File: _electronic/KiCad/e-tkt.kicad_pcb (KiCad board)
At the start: 2 copper layers, 96 x 72.7 mm, 96 parts, among them J1 USB4105-GF-A, Q1 SS8050-G, Q2 SS8050-G, U1 USB6B1, U2 AZ1117I-3.3, U3 FT231XS, U4 ESP32-WROOM-32

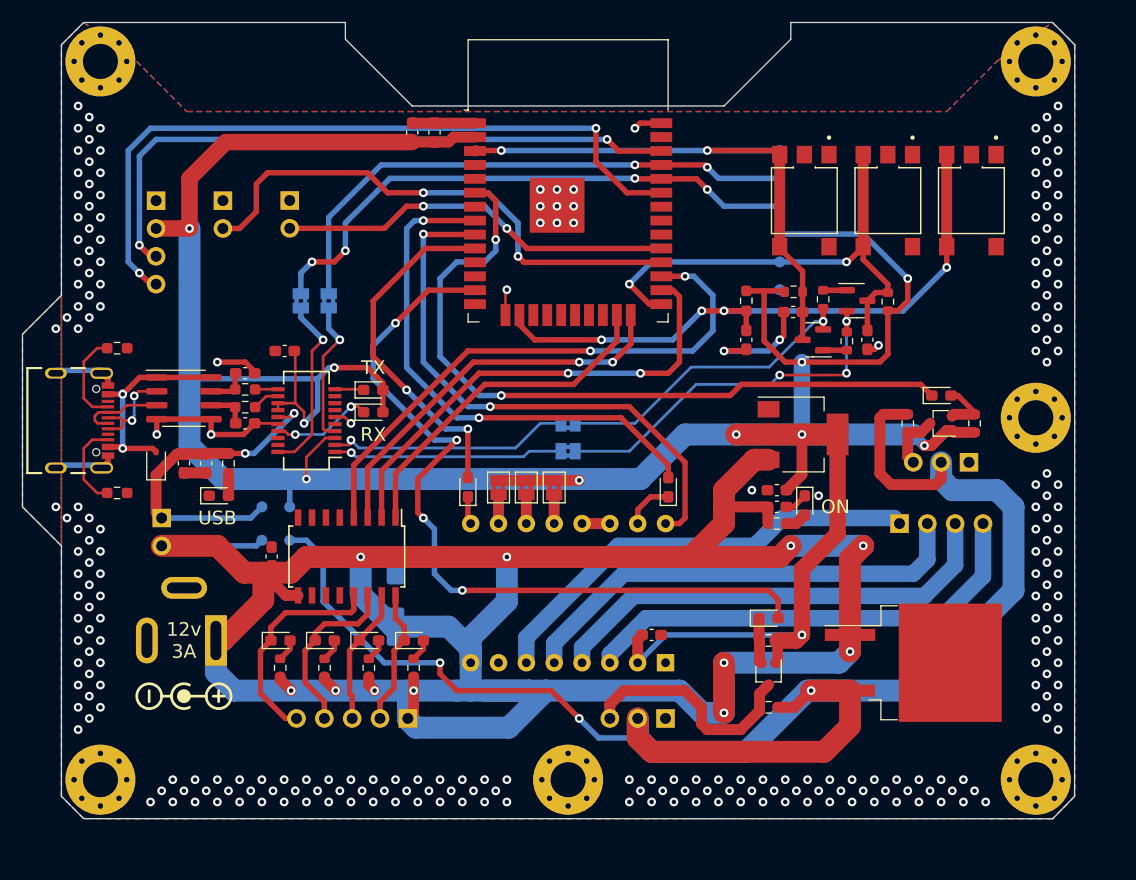
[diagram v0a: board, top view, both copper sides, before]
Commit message: board dimensions, taller
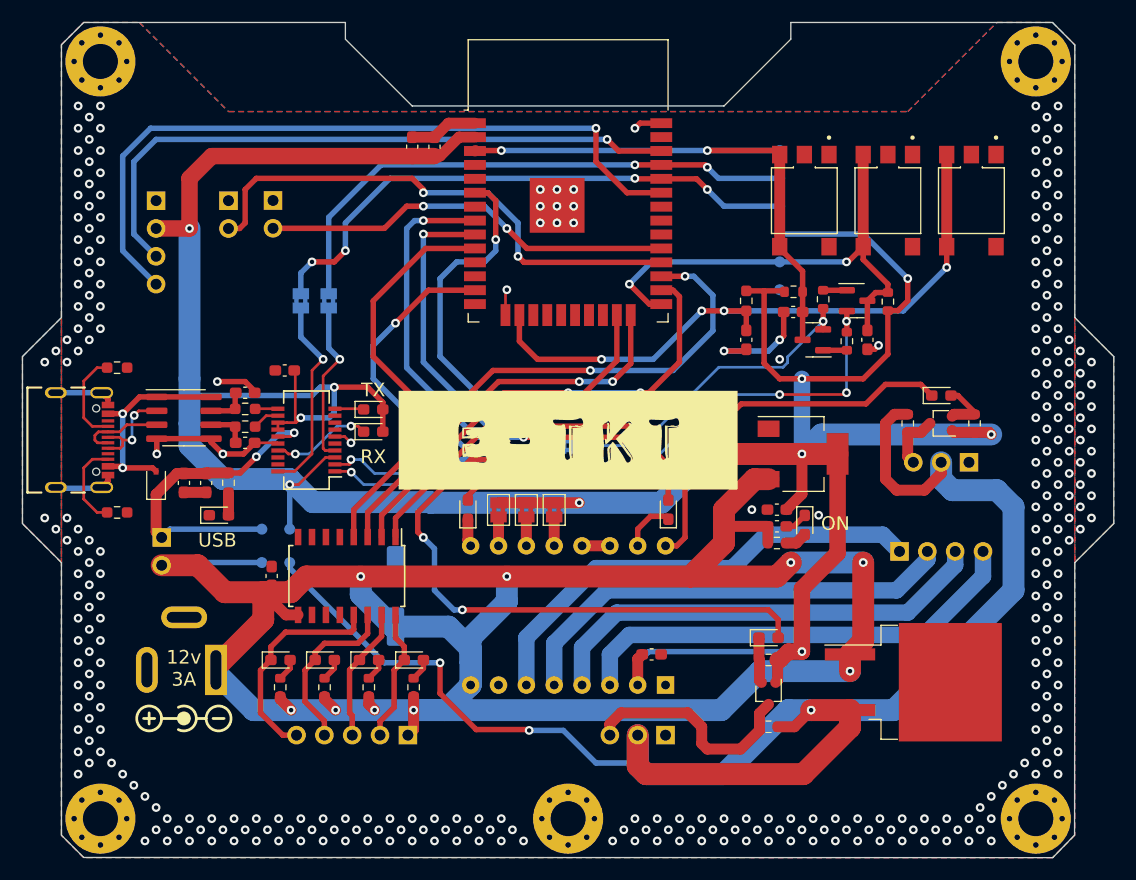
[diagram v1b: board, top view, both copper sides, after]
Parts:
- removed H5: MountingHole_Pad, MountingHole:MountingHole_3.2mm_M3_Pad_Via
- added G***: LOGO, LOGO, F.Cu at (178.3, -189.5)
- moved H3 3.56 mm to (221.0, -154.9)
- moved H4 3.56 mm to (135.6, -154.9)
- moved H6 3.56 mm to (178.3, -154.9)
- moved J_masterpower1 2.68 mm to (146.2, -168.5)
- moved J_17HS4023_1 2.54 mm to (208.5, -179.3)
- moved D1 2.04 mm to (187.5, -183.1)
- moved D4 2.04 mm to (169.2, -183.1)
- moved JP1 2.04 mm to (172.0, -183.1)
- moved JP2 2.04 mm to (174.5, -183.1)
- moved JP3 2.04 mm to (177.0, -183.1)
- moved JP6 2.03 mm to (178.3, -189.0)
- moved TP_12v1 2.03 mm to (150.4, -178.3)
- moved TP_3.3v1 2.03 mm to (152.9, -181.4)
- moved TP_5v1 2.03 mm to (150.4, -181.4)
- moved TP_6v1 2.03 mm to (152.9, -178.3)
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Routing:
- net +12V: track 243.5 -> 221.5 mm, vias 11 -> 9
- net +3.3V: track 292.5 -> 301.7 mm
- net IO25 NEMA ENA: track 31.7 -> 39.8 mm
- net IO14 SERVO: track 72.7 -> 80.6 mm
- net IO13 WIFI RST: track 57.2 -> 59.6 mm
- net DTR: track 34.4 -> 36.2 mm
- net Net-(A_DRIVER1-Pad6): track 41.1 -> 42.9 mm
- net Net-(JP4-Pad1): track 16.6 -> 18.3 mm
- net Net-(JP5-Pad1): track 13.2 -> 15.0 mm
- net IO5 LED END: track 36.3 -> 37.9 mm
- net IO34 HALL: track 67.2 -> 68.7 mm
- net RTS: track 28.4 -> 29.5 mm
- net IO33 NEMA DIR: track 51.1 -> 52.0 mm
- net IO32 NEMA STEP: track 47.9 -> 48.7 mm
- net IO16 ULN 4: track 51.3 -> 50.7 mm
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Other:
- board size 96 x 72.7 mm -> 99.6 x 76.2 mm
- board text added: "2022/07/09"
- board text added: "Andrei Speridião"
- board text added: "v0.9"
- board text removed: "Andrei Speridião 2022/07/09 v0.9"

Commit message: improved decouple caps position, routing
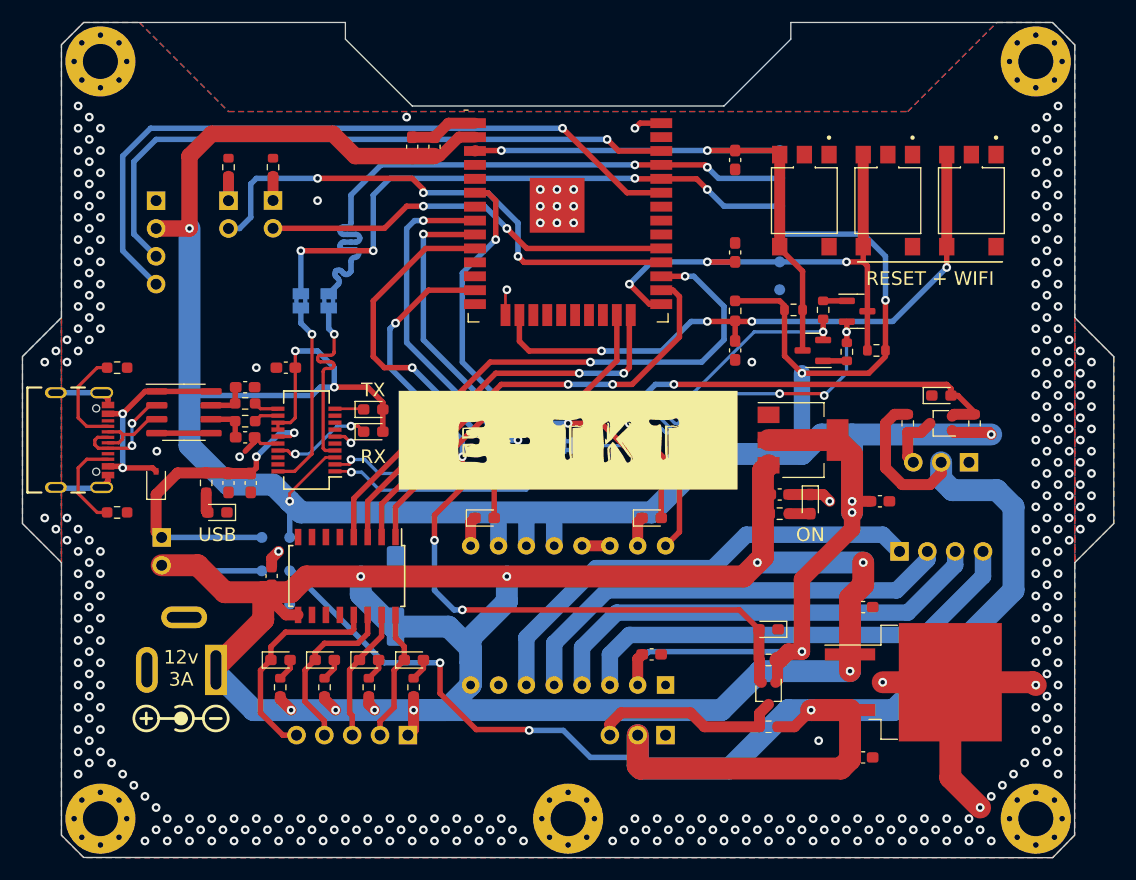
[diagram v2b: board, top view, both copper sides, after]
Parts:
- removed JP1, JP2, JP3: SolderJumper_2_Bridged, Jumper:SolderJumper-2_P1.3mm_Bridged2Bar_Pad1.0x1.5mm
- added C14: 0.33uF, Capacitor_SMD:C_0603_1608Metric_Pad1.08x0.95mm_HandSolder, F.Cu at (205.2, -174.2)
- added C17: 0.1uF, Capacitor_SMD:C_0603_1608Metric_Pad1.08x0.95mm_HandSolder, F.Cu at (205.2, -160.5)
- added R20: 0R, Resistor_SMD:R_0603_1608Metric, F.Cu at (147.3, -214.4)
- added R21: 0R, Resistor_SMD:R_0603_1608Metric, F.Cu at (151.4, -214.4)
- moved C4 14.8 mm to (193.5, -215.0), turned to 90 degrees
- moved C3 14.5 mm to (193.5, -206.6), turned to -90 degrees
- moved C11 9.43 mm to (206.8, -183.9), turned to 0 degrees
- moved R5 4.58 mm to (206.4, -197.7), turned to 180 degrees
- moved C15 4.06 mm to (149.4, -185.6)
- moved C2 4.06 mm to (147.3, -185.6)
- moved C10 2.92 mm to (197.6, -184.5)
- moved R2 2.69 mm to (197.6, -182.8)
- moved C6 2.03 mm to (164.1, -216.3)
- moved C7 2.03 mm to (166.1, -216.3)
- moved R6 2.03 mm to (145.3, -185.6)
- moved D11 1.97 mm to (200.4, -183.6)
- moved D1 1.70 mm to (185.9, -182.4), turned to 0 degrees
- moved D4 1.70 mm to (170.7, -182.4), turned to 0 degrees
- moved R1 1.65 mm to (198.9, -201.4)
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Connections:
- A_DRIVER1 pad 10: Net-(A_DRIVER1-Pad10) -> +3.3V
- A_DRIVER1 pad 11: Net-(A_DRIVER1-Pad11) -> +3.3V
- A_DRIVER1 pad 12: Net-(A_DRIVER1-Pad12) -> +3.3V
- D10 pad 1: Net-(D10-Pad1) -> GNDREF
- D9 pad 1: IO34 HALL -> GNDREF
- D9 pad 2: Net-(D9-Pad2) -> IO34 HALL
- J_LED_END1 pad 1: GNDREF -> Net-(J_LED_END1-Pad1)
- J_LED_PRESS1 pad 1: GNDREF -> Net-(J_LED_PRESS1-Pad1)
- Q_HALL1 pad 2: Net-(D9-Pad2) -> IO34 HALL
- Q_SERVO1 pad 2: Net-(D10-Pad1) -> IO14 SERVO
- R11 pad 1: Net-(D9-Pad2) -> IO34 HALL
- R13 pad 1: Net-(D10-Pad1) -> IO14 SERVO
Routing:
- net +12V: track 221.5 -> 212.9 mm
- net GNDREF: track 57.2 -> 65.2 mm, vias 328 -> 325
- net IO14 SERVO: track 80.6 -> 72.9 mm
- net RTS: track 29.5 -> 37.1 mm
- net IO1 TXD: track 50.6 -> 57.3 mm
- net Net-(D9-Pad2): track 5.09 -> 0.00 mm
- net Net-(D10-Pad1): track 4.17 -> 0.00 mm
- net SERVO: track 20.8 -> 18.0 mm
- net IO3 RXD: track 51.7 -> 54.4 mm
- net Net-(A_DRIVER1-Pad12): track 2.61 -> 0.00 mm
- net Net-(A_DRIVER1-Pad11): track 2.61 -> 0.00 mm
- net Net-(A_DRIVER1-Pad10): track 2.61 -> 0.00 mm
- net IO13 WIFI RST: track 59.6 -> 57.0 mm
- net IO16 ULN 4: track 50.7 -> 53.2 mm
- net Net-(JP5-Pad1): track 15.0 -> 17.4 mm
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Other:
- board text added: "RESET + WIFI"
